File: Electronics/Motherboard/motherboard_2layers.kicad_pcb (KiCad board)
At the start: 2 copper layers, 113.4 x 56 mm, 56 parts, among them J2 Conn_02x10_Odd_Even, M1 AO3400A, M2 AO3400A, M3 AO3400A, U1 AMS1117-3.3, U6 LM2576HVS-5, U8 STM32F405RGTx

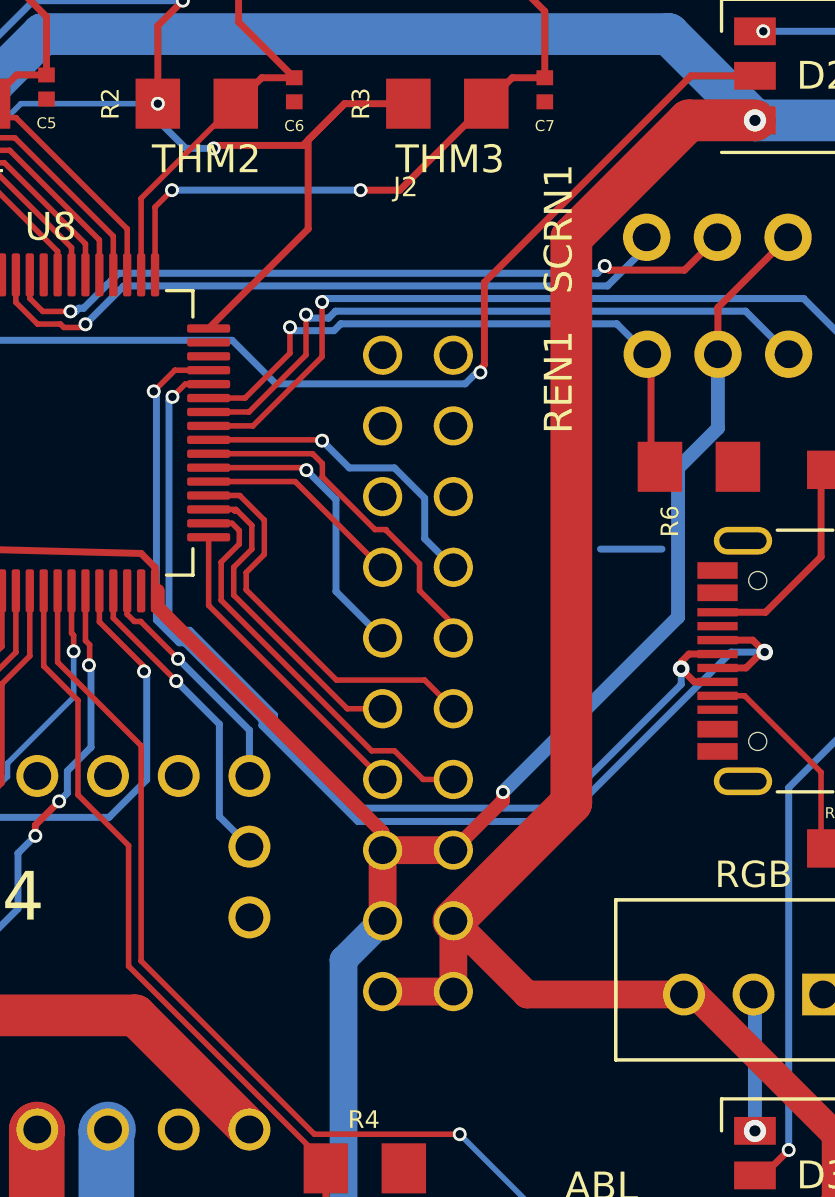
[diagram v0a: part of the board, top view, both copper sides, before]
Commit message: added models and fixed screen header footprint
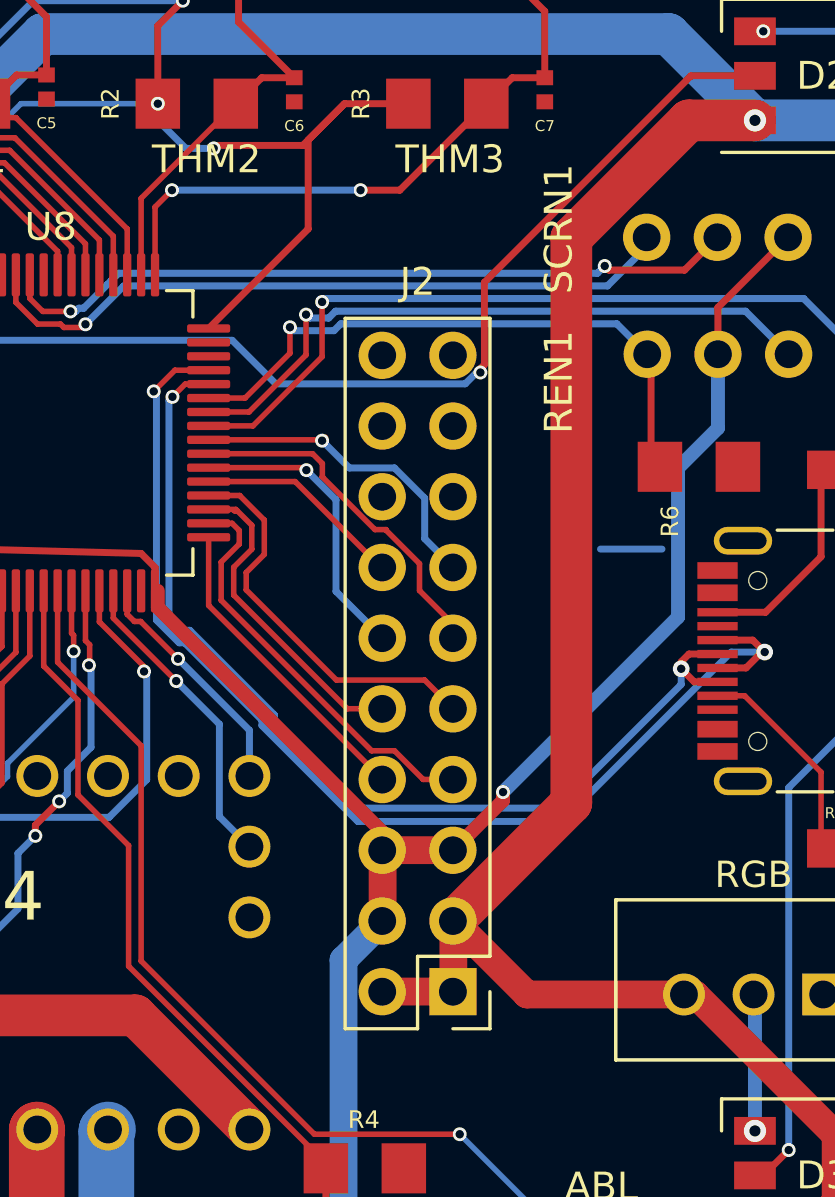
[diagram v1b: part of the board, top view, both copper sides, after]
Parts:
- J2: value Conn_02x10_Odd_Even -> PinHeader_2x10_P2.54mm_Vertical; footprint 2x10_tht:PinBox-2.54-02x10-THT -> Connector_PinHeader_2.54mm:PinHeader_2x10_P2.54mm_Vertical
- moved J2 11.5 mm to (196.2, 112.4)
- moved G*** 6.95 mm to (156.5, 90.5), turned to 135 degrees
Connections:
- J2 pad 1: +5V -> (no net)
- J2 pad 10: PB14 -> (no net)
- J2 pad 11: PC8 -> (no net)
- J2 pad 12: PC7 -> (no net)
- J2 pad 13: PC9 -> (no net)
- J2 pad 14: PC6 -> (no net)
- J2 pad 15: GNDREF -> (no net)
- J2 pad 16: GNDREF -> (no net)
- J2 pad 17: GNDREF -> (no net)
- J2 pad 18: GNDREF -> (no net)
- J2 pad 19: GNDREF -> (no net)
- J2 pad 2: +5V -> (no net)
- J2 pad 20: GNDREF -> (no net)
- J2 pad 3: +5V -> (no net)
- J2 pad 4: +3V3 -> (no net)
- J2 pad 5: +3V3 -> (no net)
- J2 pad 6: +3V3 -> (no net)
- J2 pad 7: PB13 -> (no net)
- J2 pad 8: PB12 -> (no net)
- J2 pad 9: PB15 -> (no net)
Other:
- board text added: "0.1.0a"
